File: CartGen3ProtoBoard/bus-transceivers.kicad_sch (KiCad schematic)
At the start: 2 parts, among them U2 SN74AVC16827DGGR, U3 SN74AVC16827DGGR

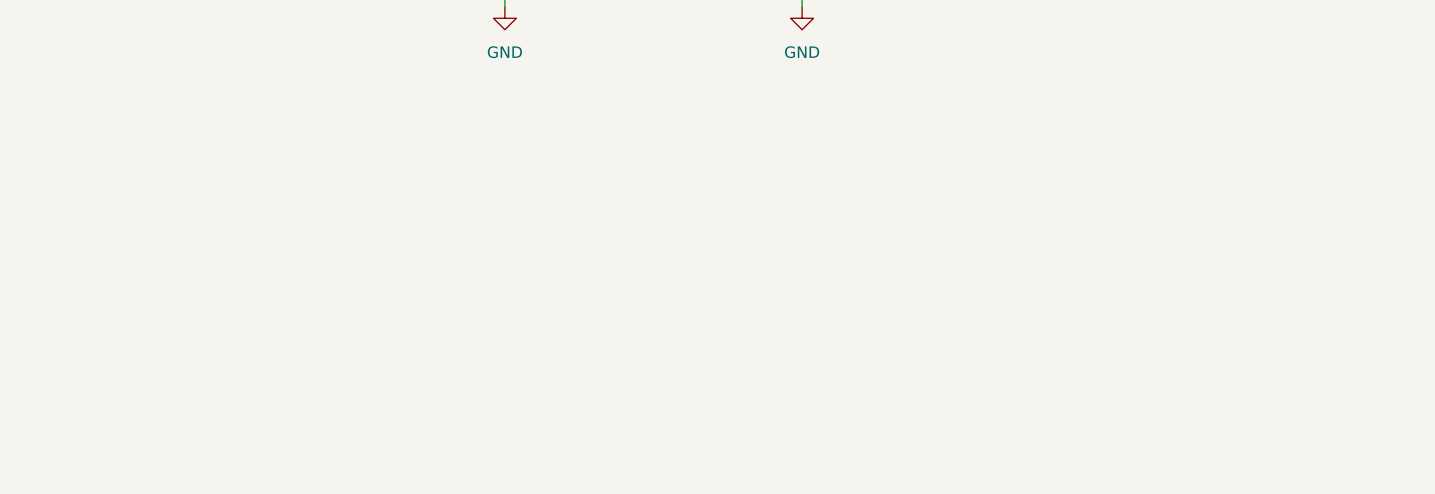
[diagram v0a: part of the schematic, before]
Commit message: Added bypass capacitors to prototype
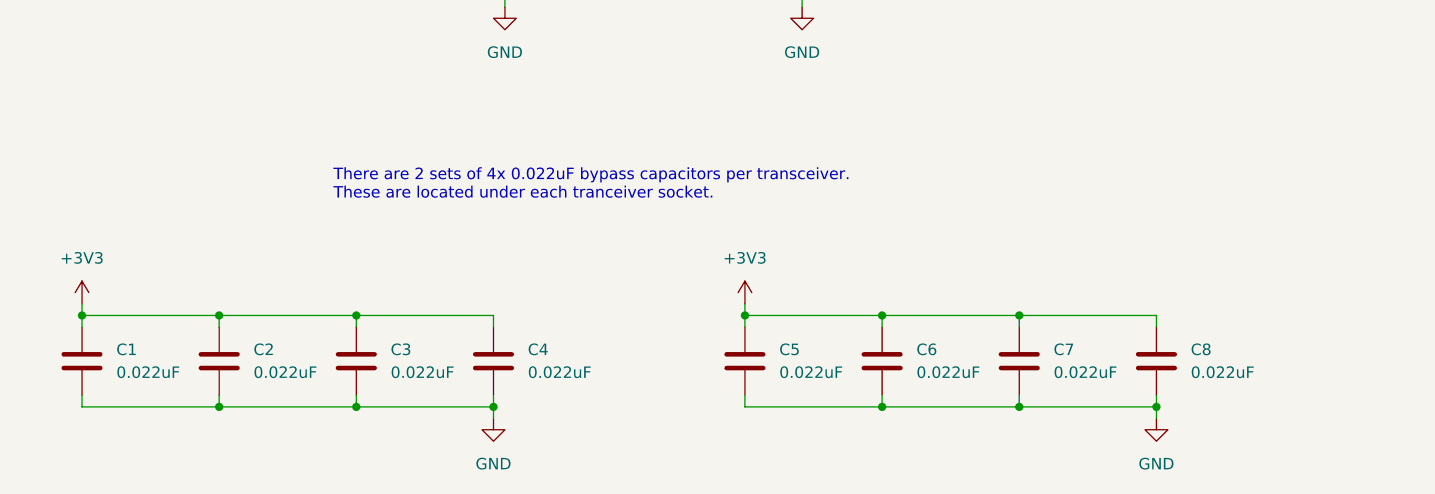
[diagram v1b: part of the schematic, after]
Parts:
- added C1, C2, C3, C4, C5, C6, C7, C8: 0.022uF, symbol Device:C
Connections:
- net +3V3: now also C1.1, C2.1, C3.1, C4.1, C5.1, C6.1, C7.1, C8.1
- net GND: now also C1.2, C2.2, C3.2, C4.2, C5.2, C6.2, C7.2, C8.2
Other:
- note added: "There are 2 sets of 4x 0.022uF bypass capacitors per transceiver. These are located under each tranceiver socket."

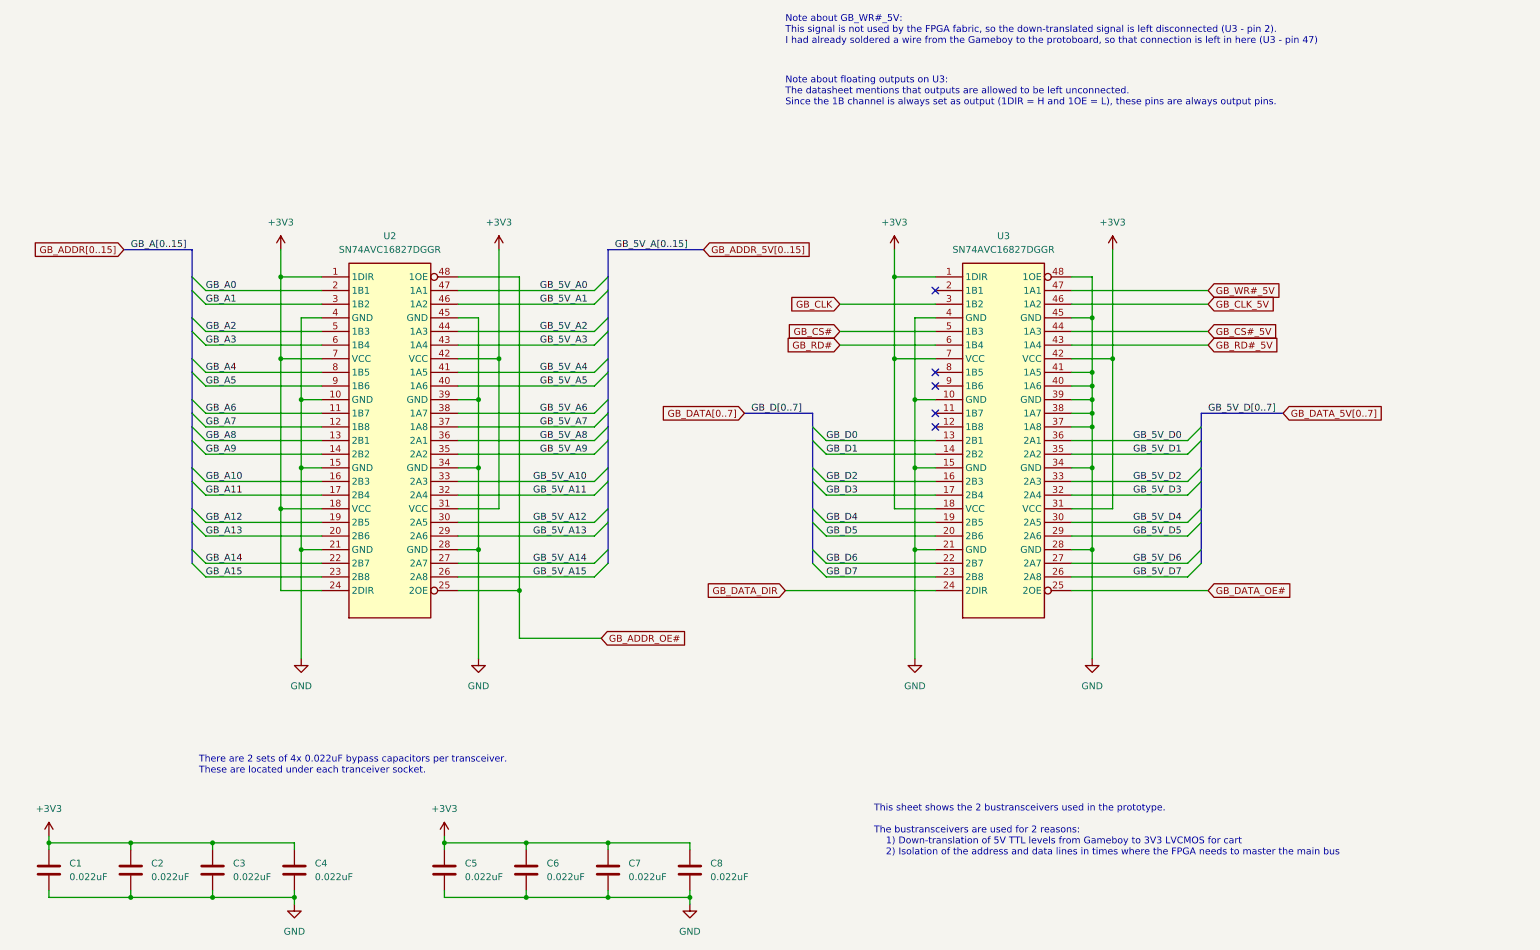
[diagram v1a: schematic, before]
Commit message: Added audio schematic
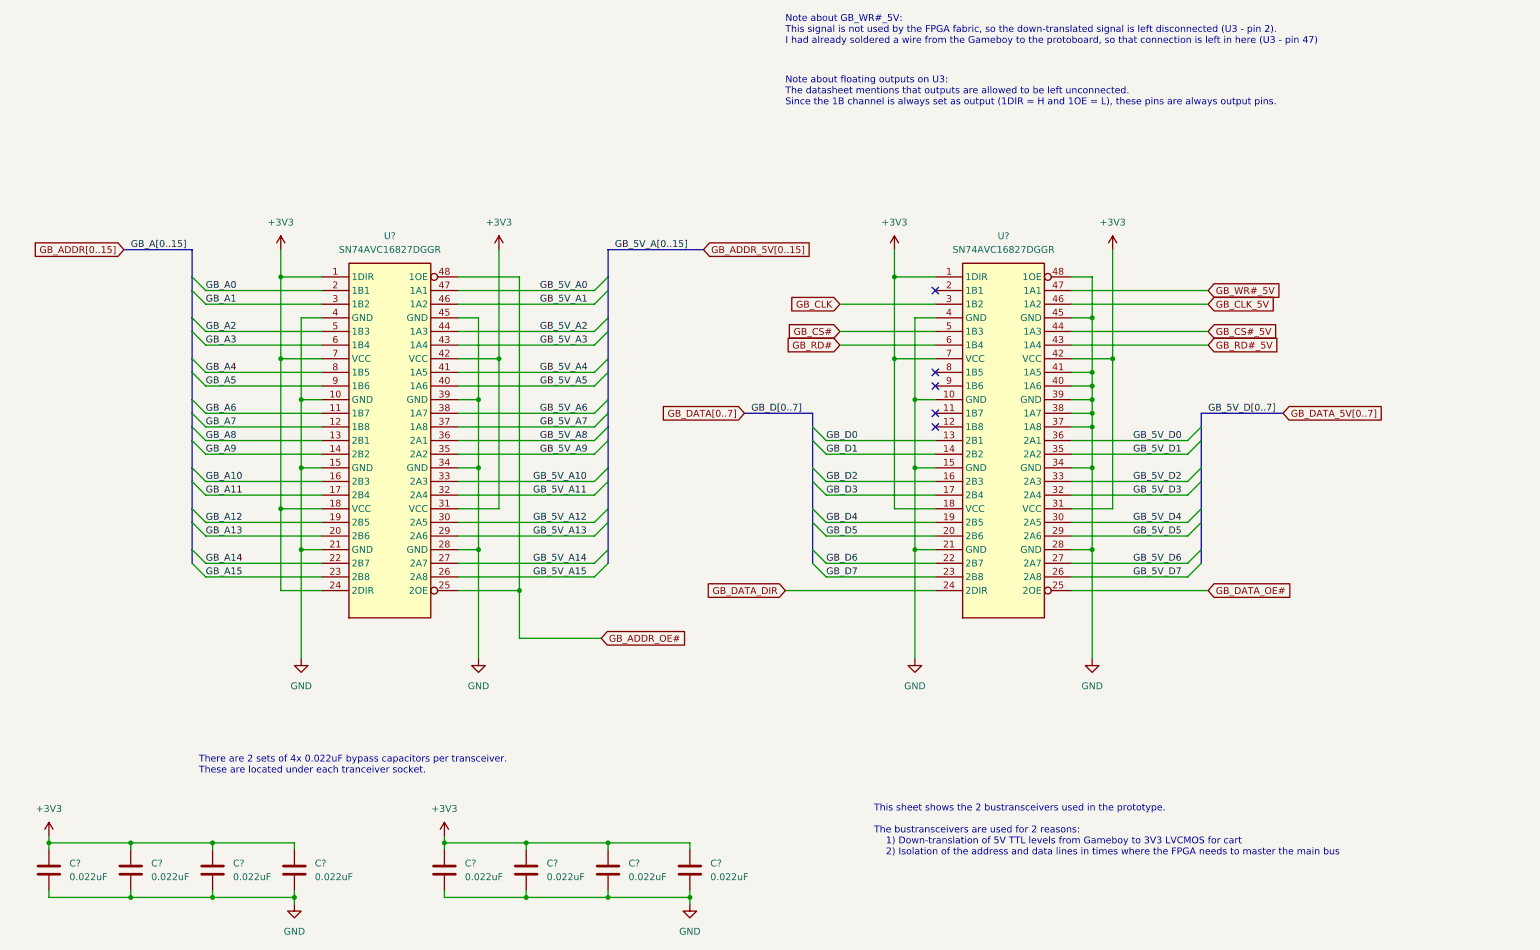
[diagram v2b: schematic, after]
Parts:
- renumbered C6 to C?, C2 to C?, C7 to C?, C8 to C?, C3 to C?, C4 to C?, C1 to C?, C5 to C?, U2 to U?, U3 to U?
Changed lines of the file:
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@@
     )
   )
-  (symbol (lib_id "Device:C") (at 114.3 180.34 0) (unit 1)
-    (in_bom yes) (on_board yes) (fields_autoplaced)
-    (property "Reference" "C6" (id 0) (at 118.11 179.0699 0)
+  (symbol (lib_id "Device:C") (at 114.3 180.34 0)
+    (in_bom yes) (on_board yes) (fields_autoplaced)
+    (property "Reference" "C?" (id 0) (at 118.11 179.0699 0)
       (effects (font (size 1.27 1.27)) (justify left))
     )
@@
     (pin "2")
   )
-  (symbol (lib_id "Device:C") (at 40.64 180.34 0) (unit 1)
-    (in_bom yes) (on_board yes) (fields_autoplaced)
-    (property "Reference" "C2" (id 0) (at 44.45 179.0699 0)
+  (symbol (lib_id "Device:C") (at 40.64 180.34 0)
+    (in_bom yes) (on_board yes) (fields_autoplaced)
+    (property "Reference" "C?" (id 0) (at 44.45 179.0699 0)
       (effects (font (size 1.27 1.27)) (justify left))
     )
@@
     (pin "2")
   )
-  (symbol (lib_id "power:+3V3") (at 223.52 64.77 0) (unit 1)
-    (in_bom yes) (on_board yes) (fields_autoplaced)
-    (property "Reference" "#PWR0113" (id 0) (at 223.52 68.58 0)
+  (symbol (lib_id "power:+3V3") (at 223.52 64.77 0)
+    (in_bom yes) (on_board yes) (fields_autoplaced)
+    (property "Reference" "#PWR?" (id 0) (at 223.52 68.58 0)
       (effects (font (size 1.27 1.27)) hide)
     )
@@
     (pin "1")
   )
-  (symbol (lib_id "power:+3V3") (at 99.06 173.99 0) (unit 1)
-    (in_bom yes) (on_board yes) (fields_autoplaced)
-    (property "Reference" "#PWR04" (id 0) (at 99.06 177.8 0)
+  (symbol (lib_id "power:+3V3") (at 99.06 173.99 0)
+    (in_bom yes) (on_board yes) (fields_autoplaced)
+    (property "Reference" "#PWR?" (id 0) (at 99.06 177.8 0)
       (effects (font (size 1.27 1.27)) hide)
     )
@@
     (pin "1")
   )
-  (symbol (lib_id "Device:C") (at 129.54 180.34 0) (unit 1)
-    (in_bom yes) (on_board yes) (fields_autoplaced)
-    (property "Reference" "C7" (id 0) (at 133.35 179.0699 0)
+  (symbol (lib_id "Device:C") (at 129.54 180.34 0)
+    (in_bom yes) (on_board yes) (fields_autoplaced)
+    (property "Reference" "C?" (id 0) (at 133.35 179.0699 0)
       (effects (font (size 1.27 1.27)) (justify left))
     )
@@
     (pin "2")
   )
-  (symbol (lib_id "Device:C") (at 144.78 180.34 0) (unit 1)
-    (in_bom yes) (on_board yes) (fields_autoplaced)
-    (property "Reference" "C8" (id 0) (at 148.59 179.0699 0)
+  (symbol (lib_id "Device:C") (at 144.78 180.34 0)
+    (in_bom yes) (on_board yes) (fields_autoplaced)
+    (property "Reference" "C?" (id 0) (at 148.59 179.0699 0)
       (effects (font (size 1.27 1.27)) (justify left))
     )
@@
     (pin "2")
   )
-  (symbol (lib_name "SN74AVC16827DGGR_1") (lib_id "74xx:SN74AVC16827DGGR") (at 88.9 100.33 0) (unit 1)
-    (in_bom yes) (on_board yes) (fields_autoplaced)
-    (property "Reference" "U2" (id 0) (at 88.9 62.23 0))
+  (symbol (lib_name "SN74AVC16827DGGR_1") (lib_id "74xx:SN74AVC16827DGGR") (at 88.9 100.33 0)
+    (in_bom yes) (on_board yes) (fields_autoplaced)
+    (property "Reference" "U?" (id 0) (at 88.9 62.23 0))
     (property "Value" "SN74AVC16827DGGR" (id 1) (at 88.9 64.77 0))
     (property "Footprint" "" (id 2) (at 58.42 134.62 0)
@@
     (pin "9")
   )
-  (symbol (lib_id "Device:C") (at 55.88 180.34 0) (unit 1)
-    (in_bom yes) (on_board yes) (fields_autoplaced)
-    (property "Reference" "C3" (id 0) (at 59.69 179.0699 0)
+  (symbol (lib_id "Device:C") (at 55.88 180.34 0)
+    (in_bom yes) (on_board yes) (fields_autoplaced)
+    (property "Reference" "C?" (id 0) (at 59.69 179.0699 0)
       (effects (font (size 1.27 1.27)) (justify left))
     )
@@
     (pin "2")
   )
-  (symbol (lib_id "power:+3V3") (at 109.22 64.77 0) (unit 1)
-    (in_bom yes) (on_board yes) (fields_autoplaced)
-    (property "Reference" "#PWR0110" (id 0) (at 109.22 68.58 0)
+  (symbol (lib_id "power:+3V3") (at 109.22 64.77 0)
+    (in_bom yes) (on_board yes) (fields_autoplaced)
+    (property "Reference" "#PWR?" (id 0) (at 109.22 68.58 0)
       (effects (font (size 1.27 1.27)) hide)
     )
@@
     (pin "1")
   )
-  (symbol (lib_id "power:GND") (at 219.71 140.97 0) (unit 1)
-    (in_bom yes) (on_board yes) (fields_autoplaced)
-    (property "Reference" "#PWR0111" (id 0) (at 219.71 147.32 0)
+  (symbol (lib_id "power:GND") (at 219.71 140.97 0)
+    (in_bom yes) (on_board yes) (fields_autoplaced)
+    (property "Reference" "#PWR?" (id 0) (at 219.71 147.32 0)
       (effects (font (size 1.27 1.27)) hide)
     )
@@
     (pin "1")
   )
-  (symbol (lib_id "power:GND") (at 72.39 140.97 0) (unit 1)
-    (in_bom yes) (on_board yes) (fields_autoplaced)
-    (property "Reference" "#PWR0109" (id 0) (at 72.39 147.32 0)
+  (symbol (lib_id "power:GND") (at 72.39 140.97 0)
+    (in_bom yes) (on_board yes) (fields_autoplaced)
+    (property "Reference" "#PWR?" (id 0) (at 72.39 147.32 0)
       (effects (font (size 1.27 1.27)) hide)
     )
@@
     (pin "1")
   )
-  (symbol (lib_id "power:+3V3") (at 25.4 173.99 0) (unit 1)
-    (in_bom yes) (on_board yes) (fields_autoplaced)
-    (property "Reference" "#PWR02" (id 0) (at 25.4 177.8 0)
+  (symbol (lib_id "power:+3V3") (at 25.4 173.99 0)
+    (in_bom yes) (on_board yes) (fields_autoplaced)
+    (property "Reference" "#PWR?" (id 0) (at 25.4 177.8 0)
       (effects (font (size 1.27 1.27)) hide)
     )
@@
     (pin "1")
   )
-  (symbol (lib_id "power:GND") (at 71.12 186.69 0) (unit 1)
-    (in_bom yes) (on_board yes) (fields_autoplaced)
-    (property "Reference" "#PWR03" (id 0) (at 71.12 193.04 0)
+  (symbol (lib_id "power:GND") (at 71.12 186.69 0)
+    (in_bom yes) (on_board yes) (fields_autoplaced)
+    (property "Reference" "#PWR?" (id 0) (at 71.12 193.04 0)
       (effects (font (size 1.27 1.27)) hide)
     )
@@
     (pin "1")
   )
-  (symbol (lib_id "power:GND") (at 186.69 140.97 0) (unit 1)
-    (in_bom yes) (on_board yes) (fields_autoplaced)
-    (property "Reference" "#PWR0112" (id 0) (at 186.69 147.32 0)
+  (symbol (lib_id "power:GND") (at 186.69 140.97 0)
+    (in_bom yes) (on_board yes) (fields_autoplaced)
+    (property "Reference" "#PWR?" (id 0) (at 186.69 147.32 0)
       (effects (font (size 1.27 1.27)) hide)
     )
@@
     (pin "1")
   )
-  (symbol (lib_id "Device:C") (at 71.12 180.34 0) (unit 1)
-    (in_bom yes) (on_board yes) (fields_autoplaced)
-    (property "Reference" "C4" (id 0) (at 74.93 179.0699 0)
+  (symbol (lib_id "Device:C") (at 71.12 180.34 0)
+    (in_bom yes) (on_board yes) (fields_autoplaced)
+    (property "Reference" "C?" (id 0) (at 74.93 179.0699 0)
       (effects (font (size 1.27 1.27)) (justify left))
     )
@@
     (pin "2")
   )
-  (symbol (lib_id "power:+3V3") (at 182.88 64.77 0) (unit 1)
-    (in_bom yes) (on_board yes) (fields_autoplaced)
-    (property "Reference" "#PWR0114" (id 0) (at 182.88 68.58 0)
+  (symbol (lib_id "power:+3V3") (at 182.88 64.77 0)
+    (in_bom yes) (on_board yes) (fields_autoplaced)
+    (property "Reference" "#PWR?" (id 0) (at 182.88 68.58 0)
       (effects (font (size 1.27 1.27)) hide)
     )
@@
     (pin "1")
   )
-  (symbol (lib_id "Device:C") (at 25.4 180.34 0) (unit 1)
-    (in_bom yes) (on_board yes) (fields_autoplaced)
-    (property "Reference" "C1" (id 0) (at 29.21 179.0699 0)
+  (symbol (lib_id "Device:C") (at 25.4 180.34 0)
+    (in_bom yes) (on_board yes) (fields_autoplaced)
+    (property "Reference" "C?" (id 0) (at 29.21 179.0699 0)
       (effects (font (size 1.27 1.27)) (justify left))
     )
@@
     (pin "2")
   )
-  (symbol (lib_id "power:GND") (at 105.41 140.97 0) (unit 1)
-    (in_bom yes) (on_board yes) (fields_autoplaced)
-    (property "Reference" "#PWR0108" (id 0) (at 105.41 147.32 0)
+  (symbol (lib_id "power:GND") (at 105.41 140.97 0)
+    (in_bom yes) (on_board yes) (fields_autoplaced)
+    (property "Reference" "#PWR?" (id 0) (at 105.41 147.32 0)
       (effects (font (size 1.27 1.27)) hide)
     )
@@
     (pin "1")
   )
-  (symbol (lib_id "74xx:SN74AVC16827DGGR") (at 203.2 100.33 0) (unit 1)
-    (in_bom yes) (on_board yes) (fields_autoplaced)
-    (property "Reference" "U3" (id 0) (at 203.2 62.23 0))
+  (symbol (lib_id "74xx:SN74AVC16827DGGR") (at 203.2 100.33 0)
+    (in_bom yes) (on_board yes) (fields_autoplaced)
+    (property "Reference" "U?" (id 0) (at 203.2 62.23 0))
     (property "Value" "SN74AVC16827DGGR" (id 1) (at 203.2 64.77 0))
     (property "Footprint" "" (id 2) (at 172.72 134.62 0)
@@
     (pin "9")
   )
-  (symbol (lib_id "Device:C") (at 99.06 180.34 0) (unit 1)
-    (in_bom yes) (on_board yes) (fields_autoplaced)
-    (property "Reference" "C5" (id 0) (at 102.87 179.0699 0)
+  (symbol (lib_id "Device:C") (at 99.06 180.34 0)
+    (in_bom yes) (on_board yes) (fields_autoplaced)
+    (property "Reference" "C?" (id 0) (at 102.87 179.0699 0)
       (effects (font (size 1.27 1.27)) (justify left))
     )
@@
     (pin "2")
   )
-  (symbol (lib_id "power:GND") (at 144.78 186.69 0) (unit 1)
-    (in_bom yes) (on_board yes) (fields_autoplaced)
-    (property "Reference" "#PWR05" (id 0) (at 144.78 193.04 0)
+  (symbol (lib_id "power:GND") (at 144.78 186.69 0)
+    (in_bom yes) (on_board yes) (fields_autoplaced)
+    (property "Reference" "#PWR?" (id 0) (at 144.78 193.04 0)
       (effects (font (size 1.27 1.27)) hide)
     )
@@
     (pin "1")
   )
-  (symbol (lib_id "power:+3V3") (at 68.58 64.77 0) (unit 1)
-    (in_bom yes) (on_board yes) (fields_autoplaced)
-    (property "Reference" "#PWR0107" (id 0) (at 68.58 68.58 0)
-      (effects (font (size 1.27 1.27)) hide)
-    )
+  (symbol (lib_id "power:+3V3") (at 68.58 64.77 0)
+    (in_bom yes) (on_board yes) (fields_autoplaced)
+    (property "Reference" "#PWR?" (id 0) (at 68.58 68.58 0)
+      (effects (font (size 1.27 1.27)) hide)
+    )
